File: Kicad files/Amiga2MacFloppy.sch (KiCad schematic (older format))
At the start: 11 parts, among them J1 DB23F, J2 Conn_02x10_Odd_Even_MountingP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, J3 DB23M, J5 DB19M, U1 74LS139, U2 74LS393

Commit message: Added the DB19M to IDC2x10 Adapter
Adapter to connect Mac Drives via DB19
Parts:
- J1: footprint A-Max:DSUB-23_Female_EdgeMount_P2.77mm -> Amiga2MacFloppy:DSUB-23_Female_EdgeMount_P2.77mm
- J3: footprint A-Max:DSUB-23_Male_EdgeMount_P2.77mm -> Amiga2MacFloppy:DSUB-23_Male_EdgeMount_P2.77mm
- J5: footprint (none) -> Amiga2MacFloppy:DSUB-19_Male_EdgeMount_P2.77mm; symbol Aimga2MacFloppy:DB19_Male_MountingHoles -> Amiga2MacFloppy:DB19_Male_MountingHoles
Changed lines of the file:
@@
 F 0 "J1" H 2330 4502 50  0000 L CNN
 F 1 "DB23F" H 2330 4411 50  0000 L CNN
-F 2 "A-Max:DSUB-23_Female_EdgeMount_P2.77mm" H 2150 4500 50  0001 C CNN
+F 2 "Amiga2MacFloppy:DSUB-23_Female_EdgeMount_P2.77mm" H 2150 4500 50  0001 C CNN
 F 3 " ~" H 2150 4500 50  0001 C CNN
 	1    2150 4500
@@
 F 0 "J3" H 9680 4264 50  0000 L CNN
 F 1 "DB23M" H 9680 4173 50  0000 L CNN
-F 2 "A-Max:DSUB-23_Male_EdgeMount_P2.77mm" H 9500 4350 50  0001 C CNN
+F 2 "Amiga2MacFloppy:DSUB-23_Male_EdgeMount_P2.77mm" H 9500 4350 50  0001 C CNN
 F 3 " ~" H 9500 4350 50  0001 C CNN
 	1    9500 4350
@@
 	5550 2200 5350 2200
 $Comp
-L Aimga2MacFloppy:DB19_Male_MountingHoles J5
+L Amiga2MacFloppy:DB19_Male_MountingHoles J5
 U 1 1 60A6B7CA
 P 2150 1600
 F 0 "J5" H 2330 1359 50  0000 L CNN
 F 1 "DB19M" H 2330 1268 50  0000 L CNN
-F 2 "" H 2150 1600 50  0001 C CNN
+F 2 "Amiga2MacFloppy:DSUB-19_Male_EdgeMount_P2.77mm" H 2150 1600 50  0001 C CNN
 F 3 " ~" H 2150 1600 50  0001 C CNN
 	1    2150 1600

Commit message: Corrections
Corrected Adapter to Female connector instead of male.
Removed R1
Cleaned up schematics
Added Open Hardware Logo
Cleaned up silkscreens
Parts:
- removed J5: DB19M, Amiga2MacFloppy:DSUB-19_Male_EdgeMount_P2.77mm, symbol Amiga2MacFloppy:DB19_Male_MountingHoles
- removed R460: R1, Resistor_THT:R_Axial_DIN0204_L3.6mm_D1.6mm_P7.62mm_Horizontal, symbol Device:R
- J2: symbol Connector_Generic_MountingPin:Conn_02x10_Odd_Even_MountingPin -> Amiga2MacFloppy:Conn_02x10_Odd_Even
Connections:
- net _INDEX: no longer J3.22 (P22)
- no-connect marks 2 -> 19
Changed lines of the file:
@@
 	8700 4950 8700 5150
 Wire Wire Line
-	8700 5700 8700 5600
-Wire Wire Line
 	8700 4350 9200 4350
 Wire Wire Line
@@
 Wire Wire Line
 	9200 3450 8700 3450
-Text GLabel 9200 3650 0    50   Input ~ 0
-_INDEX
 Text GLabel 9200 3850 0    50   Input ~ 0
 _SEL1
@@
 Text GLabel 1850 5100 0    50   Input ~ 0
 _DRES
-Text GLabel 8400 3850 0    50   Input ~ 0
+Text GLabel 9200 3950 0    50   Input ~ 0
 _SEL2
 Text GLabel 1850 5000 0    50   Input ~ 0
@@
 _Enbl2
 Wire Wire Line
-	8450 4150 8450 5600
-Wire Wire Line
-	8450 5600 8700 5600
-Connection ~ 8700 5600
-Wire Wire Line
-	8700 5600 8700 5150
-Wire Wire Line
-	8400 3850 8450 3850
-Wire Wire Line
-	8450 3600 8800 3600
-Wire Wire Line
-	8800 3600 8800 3950
-Wire Wire Line
-	8800 3950 9200 3950
-Connection ~ 8450 3850
-Wire Wire Line
-	8450 3600 8450 3850
-Wire Wire Line
 	3500 2300 3500 2200
 Wire Wire Line
@@
 Wire Wire Line
 	3500 2300 3600 2300
-$Comp
-L Device:R R460
-U 1 1 6094BB23
-P 8450 4000
-F 0 "R460" H 8520 4046 50  0000 L CNN
-F 1 "R1" H 8520 3955 50  0000 L CNN
-F 2 "Resistor_THT:R_Axial_DIN0204_L3.6mm_D1.6mm_P7.62mm_Horizontal" V 8380 4000 50  0001 C CNN
-F 3 "~" H 8450 4000 50  0001 C CNN
-	1    8450 4000
-	1    0    0    -1
-$EndComp
 $Comp
 L Connector:DB23_Female_MountingHoles J1
@@
 F 1 "DB23F" H 2330 4411 50  0000 L CNN
 F 2 "Amiga2MacFloppy:DSUB-23_Female_EdgeMount_P2.77mm" H 2150 4500 50  0001 C CNN
-F 3 " ~" H 2150 4500 50  0001 C CNN
+F 3 "https://www.tindie.com/products/retronicdesign/db23-female-connector-for-amiga-video-cables/" H 2150 4500 50  0001 C CNN
 	1    2150 4500
 	1    0    0    -1
@@
 F 1 "DB23M" H 9680 4173 50  0000 L CNN
 F 2 "Amiga2MacFloppy:DSUB-23_Male_EdgeMount_P2.77mm" H 9500 4350 50  0001 C CNN
-F 3 " ~" H 9500 4350 50  0001 C CNN
+F 3 " https://www.elliottelectronicsupply.com/connectors/db23-male-db23m-solder-cup-connector.html" H 9500 4350 50  0001 C CNN
 	1    9500 4350
 	1    0    0    -1
@@
 _DKRD
 $Comp
-L Connector_Generic_MountingPin:Conn_02x10_Odd_Even_MountingPin J2
+L Amiga2MacFloppy:Conn_02x10_Odd_Even J2
 U 1 1 608B805B
 P 3800 2000
@@
 Text GLabel 4100 2200 2    50   Input ~ 0
 _ENABLE
-Text GLabel 4700 2500 2    50   Input ~ 0
-PWM
 Text GLabel 5350 1600 0    50   Input ~ 0
 PH0
@@
 Wire Wire Line
 	5550 2200 5350 2200
-$Comp
-L Amiga2MacFloppy:DB19_Male_MountingHoles J5
-U 1 1 60A6B7CA
-P 2150 1600
-F 0 "J5" H 2330 1359 50  0000 L CNN
-F 1 "DB19M" H 2330 1268 50  0000 L CNN
-F 2 "Amiga2MacFloppy:DSUB-19_Male_EdgeMount_P2.77mm" H 2150 1600 50  0001 C CNN
-F 3 " ~" H 2150 1600 50  0001 C CNN
-	1    2150 1600
-	1    0    0    -1
-$EndComp
-$Comp
-L power:GND #PWR0111
-U 1 1 60A6F2DB
-P 1450 2800
-F 0 "#PWR0111" H 1450 2550 50  0001 C CNN
-F 1 "GND" H 1455 2627 50  0000 C CNN
-F 2 "" H 1450 2800 50  0001 C CNN
-F 3 "" H 1450 2800 50  0001 C CNN
-	1    1450 2800
-	1    0    0    -1
-$EndComp
-$Comp
-L power:+5V #PWR0112
-U 1 1 60A6F2E1
-P 1250 1800
-F 0 "#PWR0112" H 1250 1650 50  0001 C CNN
-F 1 "+5V" H 1265 1973 50  0000 C CNN
-F 2 "" H 1250 1800 50  0001 C CNN
-F 3 "" H 1250 1800 50  0001 C CNN
-	1    1250 1800
-	1    0    0    -1
-$EndComp
-Wire Wire Line
-	1850 2800 1450 2800
-Wire Wire Line
-	1850 2600 1450 2600
-Wire Wire Line
-	1450 2600 1450 2800
-Connection ~ 1450 2800
-Wire Wire Line
-	1850 2400 1450 2400
-Wire Wire Line
-	1450 2400 1450 2600
-Connection ~ 1450 2600
-Wire Wire Line
-	1850 2200 1450 2200
-Wire Wire Line
-	1450 2200 1450 2400
-Connection ~ 1450 2400
-$Comp
-L power:-12V #PWR0117
-U 1 1 60A7F899
-P 1050 2000
-F 0 "#PWR0117" H 1050 2100 50  0001 C CNN
-F 1 "-12V" H 1065 2173 50  0000 C CNN
-F 2 "" H 1050 2000 50  0001 C CNN
-F 3 "" H 1050 2000 50  0001 C CNN
-	1    1050 2000
-	1    0    0    -1
-$EndComp
-Wire Wire Line
-	1850 2000 1050 2000
-Wire Wire Line
-	1850 1800 1250 1800
-Wire Wire Line
-	1850 1600 1450 1600
-$Comp
-L power:+12V #PWR0118
-U 1 1 60A6F2E7
-P 1450 1350
-F 0 "#PWR0118" H 1450 1200 50  0001 C CNN
-F 1 "+12V" H 1465 1523 50  0000 C CNN
-F 2 "" H 1450 1350 50  0001 C CNN
-F 3 "" H 1450 1350 50  0001 C CNN
-	1    1450 1350
-	1    0    0    -1
-$EndComp
-Wire Wire Line
-	1850 1400 1450 1400
-Wire Wire Line
-	1450 1400 1450 1350
-Wire Wire Line
-	1450 1600 1450 1400
-Connection ~ 1450 1400
-NoConn ~ 1850 1200
-Text GLabel 1850 1000 0    50   Input ~ 0
-PWM
-Text GLabel 1850 2700 0    50   Input ~ 0
-PH0
-Text GLabel 1850 2500 0    50   Input ~ 0
-PH1
-Text GLabel 1850 2300 0    50   Input ~ 0
-PH2
-Text GLabel 1850 2100 0    50   Input ~ 0
-PH3
-Text GLabel 1850 1900 0    50   Input ~ 0
-_WREQ
-Text GLabel 1850 1700 0    50   Input ~ 0
-SEL
-Text GLabel 1850 1500 0    50   Input ~ 0
-_ENABLE
-Text GLabel 1850 1300 0    50   Input ~ 0
-RD
-Text GLabel 1850 1100 0    50   Input ~ 0
-WR
 Wire Wire Line
 	4600 2350 4600 2500
 Wire Wire Line
-	4600 2500 4700 2500
-Wire Wire Line
 	4600 2500 4100 2500
-Connection ~ 4600 2500
 Wire Wire Line
 	3500 1800 3300 1800
@@
 	1    0    0    -1
 $EndComp
+NoConn ~ 1850 4800
+NoConn ~ 3600 2400
+NoConn ~ 3600 2500
+NoConn ~ 5200 3950
+NoConn ~ 5200 4050
+NoConn ~ 5200 4150
+NoConn ~ 5200 5150
+NoConn ~ 5200 5250
+NoConn ~ 5200 5350
+NoConn ~ 7850 4000
+NoConn ~ 7850 4100
+NoConn ~ 7850 4200
+NoConn ~ 6850 5100
+NoConn ~ 6850 5400
+NoConn ~ 7850 5100
+NoConn ~ 7850 5200
+NoConn ~ 7850 5300
+NoConn ~ 7850 5400
+Wire Wire Line
+	8700 5150 8700 5700
 $EndSCHEMATC

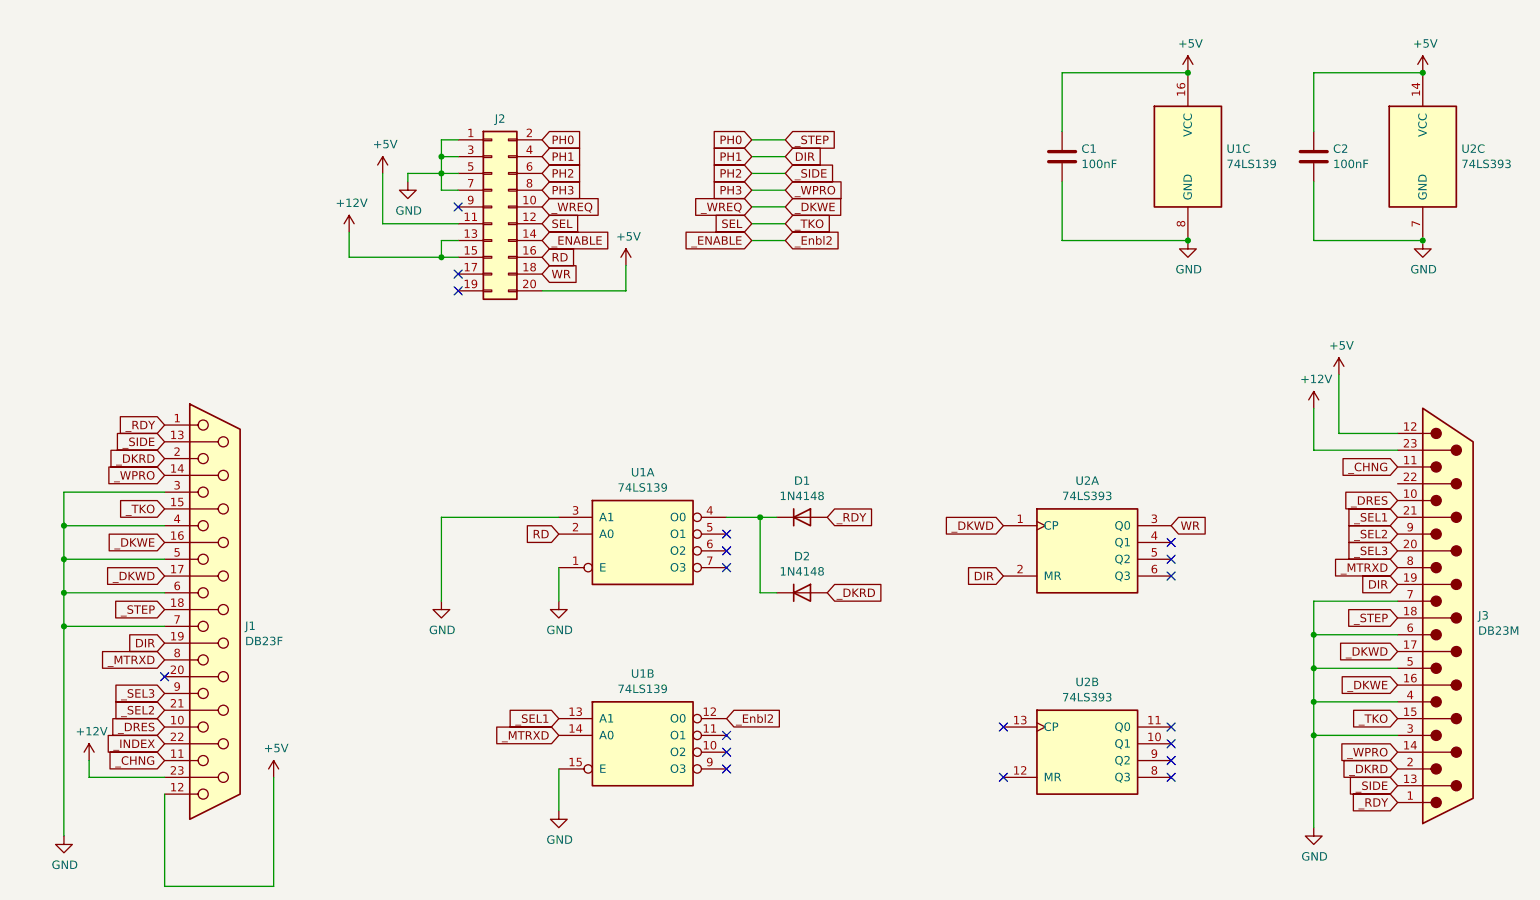
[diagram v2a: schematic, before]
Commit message: Corrections
Corrected a missing trace pin 22 of both DB23.

Updated the Gerber files.
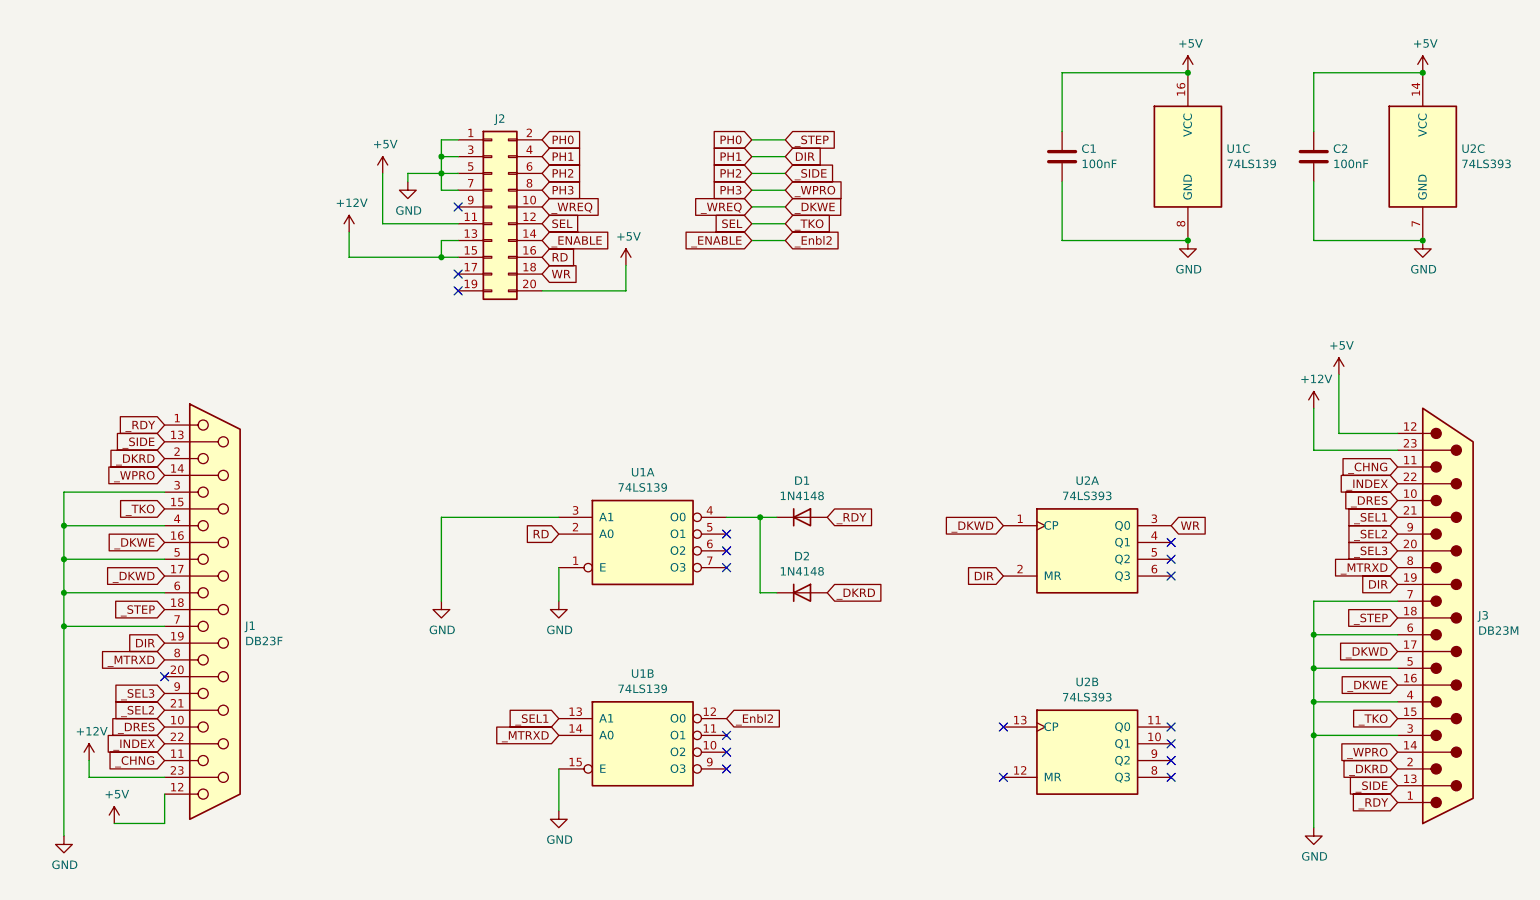
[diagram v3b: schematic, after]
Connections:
- net _INDEX: now also J3.22 (P22)
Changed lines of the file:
@@
 L power:+5V #PWR0116
 U 1 1 608DD4AC
-P 2500 5400
-F 0 "#PWR0116" H 2500 5250 50  0001 C CNN
-F 1 "+5V" H 2515 5573 50  0000 C CNN
-F 2 "" H 2500 5400 50  0001 C CNN
-F 3 "" H 2500 5400 50  0001 C CNN
-	1    2500 5400
+P 1550 5675
+F 0 "#PWR0116" H 1550 5525 50  0001 C CNN
+F 1 "+5V" H 1565 5848 50  0000 C CNN
+F 2 "" H 1550 5675 50  0001 C CNN
+F 3 "" H 1550 5675 50  0001 C CNN
+	1    1550 5675
 	1    0    0    -1
 $EndComp
@@
 Wire Wire Line
 	1250 4500 1250 5750
-Wire Wire Line
-	1850 5500 1850 6050
-Wire Wire Line
-	1850 6050 2500 6050
-Wire Wire Line
-	2500 6050 2500 5400
 Wire Wire Line
 	1250 3700 1850 3700
@@
 Wire Wire Line
 	8700 5150 8700 5700
+Text GLabel 9200 3650 0    50   Input ~ 0
+_INDEX
+Wire Wire Line
+	1550 5675 1850 5675
+Wire Wire Line
+	1850 5500 1850 5675
 $EndSCHEMATC
